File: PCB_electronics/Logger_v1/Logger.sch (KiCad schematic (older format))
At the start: 14 parts, among them P1 GPS_breakout_connector, P2 SD_breakout_connector, U1 MAX232

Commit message: schematic logger seems ok
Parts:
- added C3, C4, C5, C6: 1.0uF, symbol C
- added P10: CONN_01X03, symbol CONN_01X03
- added P11, P12, P13, P? (x2): CONN_01X02, symbol CONN_01X02
- added P8, P9: CONN_01X08, symbol CONN_01X08
- gave numbers to parts that had none: 10
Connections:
- net +5V: now also U1.16 (VCC), P13.1 (P1)
- net GND: now also U1.15 (GND), C5.1, C6.1, P13.2 (P2)
- net MISO: now also P10.3 (P3)
- net MOSI: now also P10.2 (P2)
- net SCK: now also P10.1 (P1)
- net VN_WHITE: now also U1.8 (R2IN)
- net VN_YELLOW: now also U1.7 (T2OUT)
- net ANALOG_8: now reaches XA1.A1
- net ANALOG_8: now also P8.8 (P8)
- net ANALOG_7: now reaches XA1.A2
- net ANALOG_7: now also P8.7 (P7)
- net ANALOG_6: now reaches XA1.A3
- net ANALOG_6: now also P8.6 (P6)
- net ANALOG_5: now reaches XA1.A4
- net ANALOG_5: now also P8.5 (P5)
- net ANALOG_4: now reaches XA1.A5
- net ANALOG_4: now also P8.4 (P4)
- net ANALOG_3: now reaches XA1.A6
- net ANALOG_3: now also P8.3 (P3)
- net ANALOG_2: now reaches XA1.A7
- net ANALOG_2: now also P8.2 (P2)
- net ANALOG_1: now reaches XA1.A8
- net ANALOG_1: now also P8.1 (P1)
- net RX0: now reaches XA1.D0 (D0_RX0)
- net RX0: now also P12.2 (P2)
- net TX0: now reaches XA1.D1 (D1_TX0)
- net TX0: now also P12.1 (P1)
- net TX3: now reaches XA1.D14 (D14_TX3)
- net TX3: now also U1.9 (R2OUT)
- net RX3: now reaches XA1.D15 (D15_RX3)
- net RX3: now also U1.10 (T2IN)
- net DGTL_8: now reaches XA1.D2 (D2_INT0)
- net DGTL_8: now also P9.8 (P8)
- net DGTL_7: now reaches XA1.D3 (D3_INT1)
- net DGTL_7: now also P9.7 (P7)
- net DGTL_6: now reaches XA1.D4
- net DGTL_6: now also P9.6 (P6)
- net DGTL_5: now reaches XA1.D5
- net DGTL_5: now also P9.5 (P5)
- net DGTL_4: now reaches XA1.D6
- net DGTL_4: now also P9.4 (P4)
- net DGTL_3: now reaches XA1.D7
- net DGTL_3: now also P9.3 (P3)
- net DGTL_2: now reaches XA1.D8
- net DGTL_2: now also P9.2 (P2)
- net DGTL_1: now reaches XA1.D9
- net DGTL_1: now also P9.1 (P1)
- net SCL: now reaches XA1.SCL
- net SCL: now also P11.1 (P1)
- net SDA: now reaches XA1.SDA
- net SDA: now also P11.2 (P2)
- net at U1.1 (C1+): now also C3.1
- net at U1.11 (T1IN): now also P?.2 (P2)
- net at U1.12 (R1OUT): now also P?.1 (P1)
- net at U1.13 (R1IN): now also P?.2 (P2)
- net at U1.14 (T1OUT): now also P?.1 (P1)
- net at U1.2 (V+): now also C5.2
- net at U1.3 (C1-): now also C3.2
- net at U1.4 (C2+): now also C4.1
- net at U1.5 (C2-): now also C4.2
- net at U1.6 (V-): now also C6.2
- no-connect marks 17 -> 55
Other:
- note added: "3V_logic_spare"
- note added: "5V_logic_spare"
- note added: "ADC"
- note added: "I2C"
- note added: "SPI"
- note added: "Serial 0\n(for RPi)"
- note added: "TODO: MAX232 and VN100\nTODO: pin headers SPI\nTODO: pin headers I2C\nTODO: a few AnalogPins\nTODO: a few DigitalPins"
- note added: "digital pins"
- note added: "power"
- moved on the sheet: C2, P5, P6, P7, R1, R2, U2

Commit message: schematic logger seems ok
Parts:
- gave numbers to parts that had none: 2
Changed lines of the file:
@@
 NoConn ~ 1300 3600
 $Comp
-L +5V #PWR026
+L +5V #PWR022
 U 1 1 5AF35465
 P 10100 5050
-F 0 "#PWR026" H 10100 4900 50  0001 C CNN
+F 0 "#PWR022" H 10100 4900 50  0001 C CNN
 F 1 "+5V" H 10100 5190 50  0000 C CNN
 F 2 "" H 10100 5050 50  0000 C CNN
@@
 	10100 5050 10250 5050
 $Comp
-L GND #PWR027
+L GND #PWR023
 U 1 1 5AF35551
 P 10100 5150
-F 0 "#PWR027" H 10100 4900 50  0001 C CNN
+F 0 "#PWR023" H 10100 4900 50  0001 C CNN
 F 1 "GND" H 10100 5000 50  0000 C CNN
 F 2 "" H 10100 5150 50  0000 C CNN
@@
 DGTL_8
 $Comp
-L CONN_01X02 P?
+L CONN_01X02 P14
 U 1 1 5AF3A744
 P 4900 6350
-F 0 "P?" H 4900 6500 50  0000 C CNN
+F 0 "P14" H 4900 6500 50  0000 C CNN
 F 1 "CONN_01X02" V 5000 6350 50  0000 C CNN
 F 2 "" H 4900 6350 50  0000 C CNN
@@
 5V_logic_spare
 $Comp
-L CONN_01X02 P?
+L CONN_01X02 P15
 U 1 1 5AF3AA28
 P 8350 6250
-F 0 "P?" H 8350 6400 50  0000 C CNN
+F 0 "P15" H 8350 6400 50  0000 C CNN
 F 1 "CONN_01X02" V 8450 6250 50  0000 C CNN
 F 2 "" H 8350 6250 50  0000 C CNN

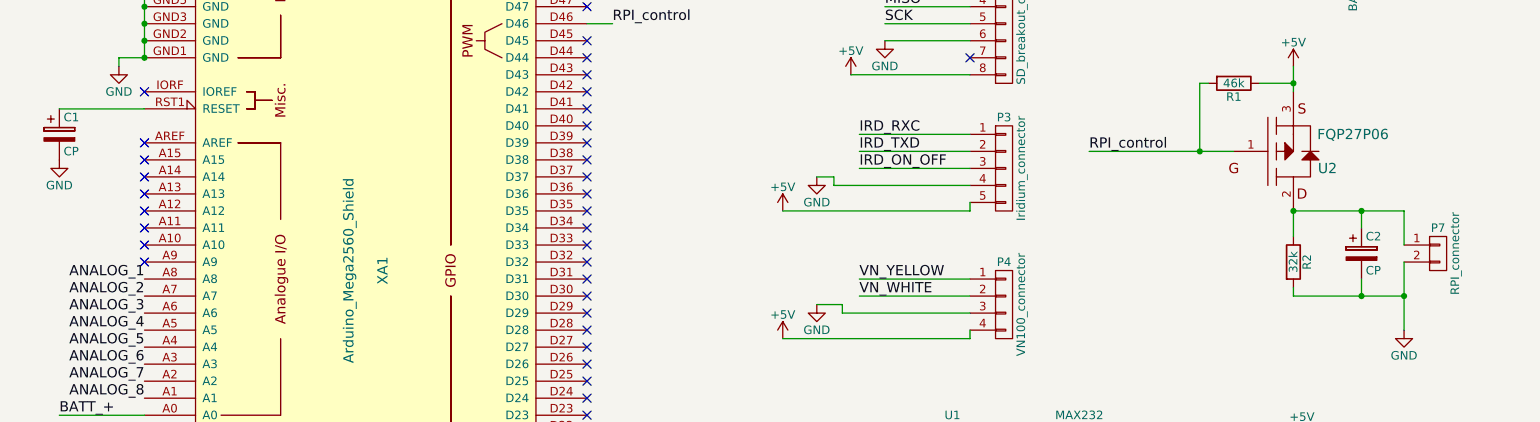
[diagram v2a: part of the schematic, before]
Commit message: placed components 1
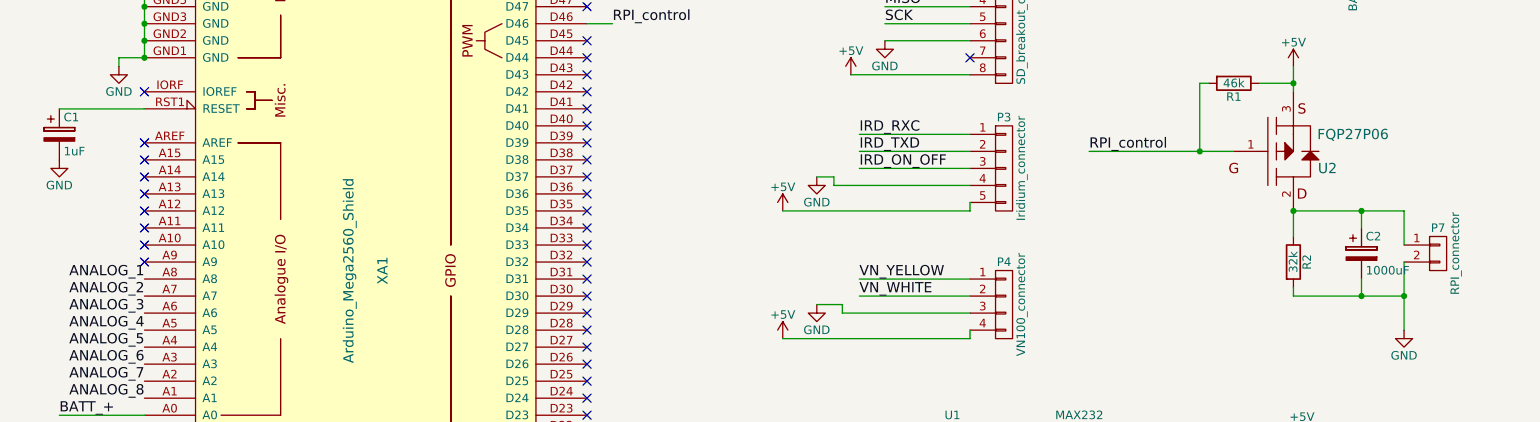
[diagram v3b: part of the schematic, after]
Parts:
- C1: value CP -> 1uF; footprint (none) -> Capacitors_ThroughHole:C_Disc_D3_P2.5
- C2: value CP -> 1000uF; footprint (none) -> Capacitors_ThroughHole:C_Disc_D3_P2.5
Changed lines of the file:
@@
 F 0 "P1" H 6350 1650 50  0000 C CNN
 F 1 "GPS_breakout_connector" V 6450 1150 50  0000 C CNN
-F 2 "" H 6350 1150 50  0000 C CNN
+F 2 "" H 6350 1150 50  0001 C CNN
 F 3 "" H 6350 1150 50  0000 C CNN
 	1    6350 1150
@@
 F 0 "P2" H 6350 2700 50  0000 C CNN
 F 1 "SD_breakout_connector" V 6450 2250 50  0000 C CNN
-F 2 "" H 6350 2250 50  0000 C CNN
+F 2 "" H 6350 2250 50  0001 C CNN
 F 3 "" H 6350 2250 50  0000 C CNN
 	1    6350 2250
@@
 F 0 "U1" H 6000 6300 50  0000 L CNN
 F 1 "MAX232" H 6650 6300 50  0000 L CNN
-F 2 "" H 6450 5450 50  0000 C CNN
+F 2 "" H 6450 5450 50  0001 C CNN
 F 3 "" H 6450 5450 50  0000 C CNN
 	1    6450 5450
@@
 F 0 "U2" H 8250 2950 60  0000 C CNN
 F 1 "FQP27P06" H 8400 3150 60  0000 C CNN
-F 2 "" H 8050 3050 60  0000 C CNN
+F 2 "" H 8050 3050 60  0001 C CNN
 F 3 "" H 8050 3050 60  0000 C CNN
 	1    8050 3050
@@
 P 800 2950
 F 0 "C1" H 825 3050 50  0000 L CNN
-F 1 "CP" H 825 2850 50  0000 L CNN
-F 2 "" H 838 2800 50  0000 C CNN
+F 1 "1uF" H 825 2850 50  0000 L CNN
+F 2 "Capacitors_ThroughHole:C_Disc_D3_P2.5" H 838 2800 50  0001 C CNN
 F 3 "" H 800 2950 50  0000 C CNN
 	1    800  2950
@@
 F 0 "P4" H 6350 4200 50  0000 C CNN
 F 1 "VN100_connector" V 6450 3950 50  0000 C CNN
-F 2 "" H 6350 3950 50  0000 C CNN
+F 2 "" H 6350 3950 50  0001 C CNN
 F 3 "" H 6350 3950 50  0000 C CNN
 	1    6350 3950
@@
 F 0 "P7" H 8900 3800 50  0000 C CNN
 F 1 "RPI_connector" V 9000 3650 50  0000 C CNN
-F 2 "" H 8900 3650 50  0000 C CNN
+F 2 "" H 8900 3650 50  0001 C CNN
 F 3 "" H 8900 3650 50  0000 C CNN
 	1    8900 3650
@@
 F 0 "P5" H 8300 1300 50  0000 C CNN
 F 1 "PowerManager_connector" V 8400 1100 50  0000 C CNN
-F 2 "" H 8300 1100 50  0000 C CNN
+F 2 "" H 8300 1100 50  0001 C CNN
 F 3 "" H 8300 1100 50  0000 C CNN
 	1    8300 1100
@@
 F 0 "P3" H 6350 3450 50  0000 C CNN
 F 1 "Iridium_connector" V 6450 3150 50  0000 C CNN
-F 2 "" H 6350 3150 50  0000 C CNN
+F 2 "" H 6350 3150 50  0001 C CNN
 F 3 "" H 6350 3150 50  0000 C CNN
 	1    6350 3150
@@
 F 0 "P6" H 8300 2050 50  0000 C CNN
 F 1 "BATT_connector" V 8400 1950 50  0000 C CNN
-F 2 "" H 8300 1950 50  0000 C CNN
+F 2 "" H 8300 1950 50  0001 C CNN
 F 3 "" H 8300 1950 50  0000 C CNN
 	1    8300 1950
@@
 P 8450 3650
 F 0 "C2" H 8475 3750 50  0000 L CNN
-F 1 "CP" H 8475 3550 50  0000 L CNN
-F 2 "" H 8488 3500 50  0000 C CNN
+F 1 "1000uF" H 8475 3550 50  0000 L CNN
+F 2 "Capacitors_ThroughHole:C_Disc_D3_P2.5" H 8488 3500 50  0001 C CNN
 F 3 "" H 8450 3650 50  0000 C CNN
 	1    8450 3650
@@
 F 0 "R1" V 7780 2650 50  0000 C CNN
 F 1 "46k" V 7700 2650 50  0000 C CNN
-F 2 "" V 7630 2650 50  0000 C CNN
+F 2 "" V 7630 2650 50  0001 C CNN
 F 3 "" H 7700 2650 50  0000 C CNN
 	1    7700 2650
@@
 F 0 "R2" V 8130 3700 50  0000 C CNN
 F 1 "32k" V 8050 3700 50  0000 C CNN
-F 2 "" V 7980 3700 50  0000 C CNN
+F 2 "" V 7980 3700 50  0001 C CNN
 F 3 "" H 8050 3700 50  0000 C CNN
 	1    8050 3700
@@
 F 0 "P8" H 10450 1700 50  0000 C CNN
 F 1 "CONN_01X08" V 10550 1250 50  0000 C CNN
-F 2 "" H 10450 1250 50  0000 C CNN
+F 2 "" H 10450 1250 50  0001 C CNN
 F 3 "" H 10450 1250 50  0000 C CNN
 	1    10450 1250
@@
 F 0 "P9" H 10450 2800 50  0000 C CNN
 F 1 "CONN_01X08" V 10550 2350 50  0000 C CNN
-F 2 "" H 10450 2350 50  0000 C CNN
+F 2 "" H 10450 2350 50  0001 C CNN
 F 3 "" H 10450 2350 50  0000 C CNN
 	1    10450 2350
@@
 F 0 "P10" H 10450 3400 50  0000 C CNN
 F 1 "CONN_01X03" V 10550 3200 50  0000 C CNN
-F 2 "" H 10450 3200 50  0000 C CNN
+F 2 "" H 10450 3200 50  0001 C CNN
 F 3 "" H 10450 3200 50  0000 C CNN
 	1    10450 3200
@@
 F 0 "P11" H 10450 4000 50  0000 C CNN
 F 1 "CONN_01X02" V 10550 3850 50  0000 C CNN
-F 2 "" H 10450 3850 50  0000 C CNN
+F 2 "" H 10450 3850 50  0001 C CNN
 F 3 "" H 10450 3850 50  0000 C CNN
 	1    10450 3850
@@
 F 0 "P13" H 10450 5250 50  0000 C CNN
 F 1 "CONN_01X02" V 10550 5100 50  0000 C CNN
-F 2 "" H 10450 5100 50  0000 C CNN
+F 2 "" H 10450 5100 50  0001 C CNN
 F 3 "" H 10450 5100 50  0000 C CNN
 	1    10450 5100
@@
 F 0 "C3" H 5475 5050 50  0000 L CNN
 F 1 "1.0uF" H 5475 4850 50  0000 L CNN
-F 2 "" H 5488 4800 50  0000 C CNN
+F 2 "" H 5488 4800 50  0001 C CNN
 F 3 "" H 5450 4950 50  0000 C CNN
 	1    5450 4950
@@
 F 0 "C4" H 5475 5550 50  0000 L CNN
 F 1 "1.0uF" H 5475 5350 50  0000 L CNN
-F 2 "" H 5488 5300 50  0000 C CNN
+F 2 "" H 5488 5300 50  0001 C CNN
 F 3 "" H 5450 5450 50  0000 C CNN
 	1    5450 5450
@@
 F 0 "C5" H 7425 5250 50  0000 L CNN
 F 1 "1.0uF" V 7250 5050 50  0000 L CNN
-F 2 "" H 7438 5000 50  0000 C CNN
+F 2 "" H 7438 5000 50  0001 C CNN
 F 3 "" H 7400 5150 50  0000 C CNN
 	1    7400 5150
@@
 F 0 "C6" H 7425 5750 50  0000 L CNN
 F 1 "1.0uF" V 7250 5550 50  0000 L CNN
-F 2 "" H 7438 5500 50  0000 C CNN
+F 2 "" H 7438 5500 50  0001 C CNN
 F 3 "" H 7400 5650 50  0000 C CNN
 	1    7400 5650
@@
 F 0 "P12" H 10450 4600 50  0000 C CNN
 F 1 "CONN_01X02" V 10550 4450 50  0000 C CNN
-F 2 "" H 10450 4450 50  0000 C CNN
+F 2 "" H 10450 4450 50  0001 C CNN
 F 3 "" H 10450 4450 50  0000 C CNN
 	1    10450 4450
@@
 F 0 "P14" H 4900 6500 50  0000 C CNN
 F 1 "CONN_01X02" V 5000 6350 50  0000 C CNN
-F 2 "" H 4900 6350 50  0000 C CNN
+F 2 "" H 4900 6350 50  0001 C CNN
 F 3 "" H 4900 6350 50  0000 C CNN
 	1    4900 6350
@@
 F 0 "P15" H 8350 6400 50  0000 C CNN
 F 1 "CONN_01X02" V 8450 6250 50  0000 C CNN
-F 2 "" H 8350 6250 50  0000 C CNN
+F 2 "" H 8350 6250 50  0001 C CNN
 F 3 "" H 8350 6250 50  0000 C CNN
 	1    8350 6250

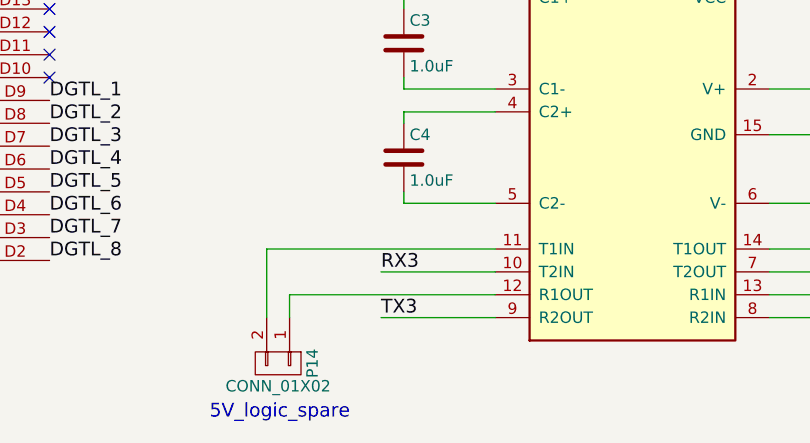
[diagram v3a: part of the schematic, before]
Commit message: corrected error on MAX232
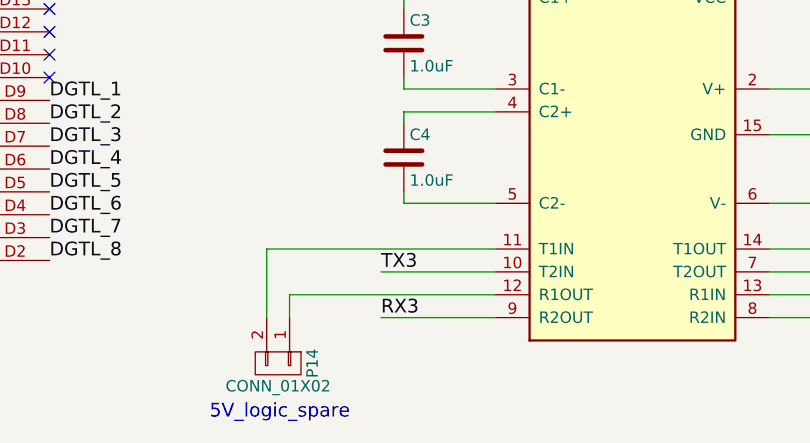
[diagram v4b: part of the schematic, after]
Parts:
- C1: footprint Capacitors_ThroughHole:C_Disc_D3_P2.5 -> Capacitors_ThroughHole:C_Radial_D8_L11.5_P3.5
- C2: footprint Capacitors_ThroughHole:C_Disc_D3_P2.5 -> Capacitors_ThroughHole:C_Radial_D8_L13_P3.8
- C3, C4, C5, C6: footprint (none) -> Capacitors_ThroughHole:C_Disc_D3_P2.5
- P1: footprint (none) -> Pin_Headers:Pin_Header_Straight_1x09
- P10, P5: footprint (none) -> Pin_Headers:Pin_Header_Straight_1x03
- P11, P12, P13, P14, P15, P7: footprint (none) -> Pin_Headers:Pin_Header_Straight_2x01
- P2, P8, P9: footprint (none) -> Pin_Headers:Pin_Header_Straight_1x08
- P3: footprint (none) -> Pin_Headers:Pin_Header_Straight_1x05
- P4: footprint (none) -> Pin_Headers:Pin_Header_Straight_1x04
- P6: footprint (none) -> Pin_Headers:Pin_Header_Straight_1x01
- R1, R2: footprint (none) -> Resistors_ThroughHole:Resistor_Horizontal_RM10mm
- U1: footprint (none) -> Housings_DIP:DIP-16_W7.62mm_LongPads
- U2: footprint (none) -> TO_SOT_Packages_THT:TO-220_Neutral123_Vertical
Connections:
- net RX3: now also U1.9 (R2OUT); no longer U1.10 (T2IN)
- net TX3: now also U1.10 (T2IN); no longer U1.9 (R2OUT)
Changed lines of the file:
@@
 F 0 "P1" H 6350 1650 50  0000 C CNN
 F 1 "GPS_breakout_connector" V 6450 1150 50  0000 C CNN
-F 2 "" H 6350 1150 50  0001 C CNN
+F 2 "Pin_Headers:Pin_Header_Straight_1x09" H 6350 1150 50  0001 C CNN
 F 3 "" H 6350 1150 50  0000 C CNN
 	1    6350 1150
@@
 F 0 "P2" H 6350 2700 50  0000 C CNN
 F 1 "SD_breakout_connector" V 6450 2250 50  0000 C CNN
-F 2 "" H 6350 2250 50  0001 C CNN
+F 2 "Pin_Headers:Pin_Header_Straight_1x08" H 6350 2250 50  0001 C CNN
 F 3 "" H 6350 2250 50  0000 C CNN
 	1    6350 2250
@@
 F 0 "U1" H 6000 6300 50  0000 L CNN
 F 1 "MAX232" H 6650 6300 50  0000 L CNN
-F 2 "" H 6450 5450 50  0001 C CNN
+F 2 "Housings_DIP:DIP-16_W7.62mm_LongPads" H 6450 5450 50  0001 C CNN
 F 3 "" H 6450 5450 50  0000 C CNN
 	1    6450 5450
@@
 F 0 "U2" H 8250 2950 60  0000 C CNN
 F 1 "FQP27P06" H 8400 3150 60  0000 C CNN
-F 2 "" H 8050 3050 60  0001 C CNN
+F 2 "TO_SOT_Packages_THT:TO-220_Neutral123_Vertical" H 8050 3050 60  0001 C CNN
 F 3 "" H 8050 3050 60  0000 C CNN
 	1    8050 3050
@@
 F 0 "C1" H 825 3050 50  0000 L CNN
 F 1 "1uF" H 825 2850 50  0000 L CNN
-F 2 "Capacitors_ThroughHole:C_Disc_D3_P2.5" H 838 2800 50  0001 C CNN
+F 2 "Capacitors_ThroughHole:C_Radial_D8_L11.5_P3.5" H 838 2800 50  0001 C CNN
 F 3 "" H 800 2950 50  0000 C CNN
 	1    800  2950
@@
 F 0 "P4" H 6350 4200 50  0000 C CNN
 F 1 "VN100_connector" V 6450 3950 50  0000 C CNN
-F 2 "" H 6350 3950 50  0001 C CNN
+F 2 "Pin_Headers:Pin_Header_Straight_1x04" H 6350 3950 50  0001 C CNN
 F 3 "" H 6350 3950 50  0000 C CNN
 	1    6350 3950
@@
 F 0 "P7" H 8900 3800 50  0000 C CNN
 F 1 "RPI_connector" V 9000 3650 50  0000 C CNN
-F 2 "" H 8900 3650 50  0001 C CNN
+F 2 "Pin_Headers:Pin_Header_Straight_2x01" H 8900 3650 50  0001 C CNN
 F 3 "" H 8900 3650 50  0000 C CNN
 	1    8900 3650
@@
 F 0 "P5" H 8300 1300 50  0000 C CNN
 F 1 "PowerManager_connector" V 8400 1100 50  0000 C CNN
-F 2 "" H 8300 1100 50  0001 C CNN
+F 2 "Pin_Headers:Pin_Header_Straight_1x03" H 8300 1100 50  0001 C CNN
 F 3 "" H 8300 1100 50  0000 C CNN
 	1    8300 1100
@@
 F 0 "P3" H 6350 3450 50  0000 C CNN
 F 1 "Iridium_connector" V 6450 3150 50  0000 C CNN
-F 2 "" H 6350 3150 50  0001 C CNN
+F 2 "Pin_Headers:Pin_Header_Straight_1x05" H 6350 3150 50  0001 C CNN
 F 3 "" H 6350 3150 50  0000 C CNN
 	1    6350 3150
@@
 F 0 "P6" H 8300 2050 50  0000 C CNN
 F 1 "BATT_connector" V 8400 1950 50  0000 C CNN
-F 2 "" H 8300 1950 50  0001 C CNN
+F 2 "Pin_Headers:Pin_Header_Straight_1x01" H 8300 1950 50  0001 C CNN
 F 3 "" H 8300 1950 50  0000 C CNN
 	1    8300 1950
@@
 F 0 "C2" H 8475 3750 50  0000 L CNN
 F 1 "1000uF" H 8475 3550 50  0000 L CNN
-F 2 "Capacitors_ThroughHole:C_Disc_D3_P2.5" H 8488 3500 50  0001 C CNN
+F 2 "Capacitors_ThroughHole:C_Radial_D8_L13_P3.8" H 8488 3500 50  0001 C CNN
 F 3 "" H 8450 3650 50  0000 C CNN
 	1    8450 3650
@@
 F 0 "R1" V 7780 2650 50  0000 C CNN
 F 1 "46k" V 7700 2650 50  0000 C CNN
-F 2 "" V 7630 2650 50  0001 C CNN
+F 2 "Resistors_ThroughHole:Resistor_Horizontal_RM10mm" V 7630 2650 50  0001 C CNN
 F 3 "" H 7700 2650 50  0000 C CNN
 	1    7700 2650
@@
 F 0 "R2" V 8130 3700 50  0000 C CNN
 F 1 "32k" V 8050 3700 50  0000 C CNN
-F 2 "" V 7980 3700 50  0001 C CNN
+F 2 "Resistors_ThroughHole:Resistor_Horizontal_RM10mm" V 7980 3700 50  0001 C CNN
 F 3 "" H 8050 3700 50  0000 C CNN
 	1    8050 3700
@@
 F 0 "P8" H 10450 1700 50  0000 C CNN
 F 1 "CONN_01X08" V 10550 1250 50  0000 C CNN
-F 2 "" H 10450 1250 50  0001 C CNN
+F 2 "Pin_Headers:Pin_Header_Straight_1x08" H 10450 1250 50  0001 C CNN
 F 3 "" H 10450 1250 50  0000 C CNN
 	1    10450 1250
@@
 F 0 "P9" H 10450 2800 50  0000 C CNN
 F 1 "CONN_01X08" V 10550 2350 50  0000 C CNN
-F 2 "" H 10450 2350 50  0001 C CNN
+F 2 "Pin_Headers:Pin_Header_Straight_1x08" H 10450 2350 50  0001 C CNN
 F 3 "" H 10450 2350 50  0000 C CNN
 	1    10450 2350
@@
 F 0 "P10" H 10450 3400 50  0000 C CNN
 F 1 "CONN_01X03" V 10550 3200 50  0000 C CNN
-F 2 "" H 10450 3200 50  0001 C CNN
+F 2 "Pin_Headers:Pin_Header_Straight_1x03" H 10450 3200 50  0001 C CNN
 F 3 "" H 10450 3200 50  0000 C CNN
 	1    10450 3200
@@
 F 0 "P11" H 10450 4000 50  0000 C CNN
 F 1 "CONN_01X02" V 10550 3850 50  0000 C CNN
-F 2 "" H 10450 3850 50  0001 C CNN
+F 2 "Pin_Headers:Pin_Header_Straight_2x01" H 10450 3850 50  0001 C CNN
 F 3 "" H 10450 3850 50  0000 C CNN
 	1    10450 3850
@@
 F 0 "P13" H 10450 5250 50  0000 C CNN
 F 1 "CONN_01X02" V 10550 5100 50  0000 C CNN
-F 2 "" H 10450 5100 50  0001 C CNN
+F 2 "Pin_Headers:Pin_Header_Straight_2x01" H 10450 5100 50  0001 C CNN
 F 3 "" H 10450 5100 50  0000 C CNN
 	1    10450 5100
@@
 	700  5200 1300 5200
 Text Label 5350 5950 0    60   ~ 0
-RX3
+TX3
 Wire Wire Line
 	5350 5950 5850 5950
 Text Label 5350 6150 0    60   ~ 0
-TX3
+RX3
 Wire Wire Line
 	5350 6150 5850 6150
@@
 F 0 "C3" H 5475 5050 50  0000 L CNN
 F 1 "1.0uF" H 5475 4850 50  0000 L CNN
-F 2 "" H 5488 4800 50  0001 C CNN
+F 2 "Capacitors_ThroughHole:C_Disc_D3_P2.5" H 5488 4800 50  0001 C CNN
 F 3 "" H 5450 4950 50  0000 C CNN
 	1    5450 4950
@@
 F 0 "C4" H 5475 5550 50  0000 L CNN
 F 1 "1.0uF" H 5475 5350 50  0000 L CNN
-F 2 "" H 5488 5300 50  0001 C CNN
+F 2 "Capacitors_ThroughHole:C_Disc_D3_P2.5" H 5488 5300 50  0001 C CNN
 F 3 "" H 5450 5450 50  0000 C CNN
 	1    5450 5450
@@
 F 0 "C5" H 7425 5250 50  0000 L CNN
 F 1 "1.0uF" V 7250 5050 50  0000 L CNN
-F 2 "" H 7438 5000 50  0001 C CNN
+F 2 "Capacitors_ThroughHole:C_Disc_D3_P2.5" H 7438 5000 50  0001 C CNN
 F 3 "" H 7400 5150 50  0000 C CNN
 	1    7400 5150
@@
 F 0 "C6" H 7425 5750 50  0000 L CNN
 F 1 "1.0uF" V 7250 5550 50  0000 L CNN
-F 2 "" H 7438 5500 50  0001 C CNN
+F 2 "Capacitors_ThroughHole:C_Disc_D3_P2.5" H 7438 5500 50  0001 C CNN
 F 3 "" H 7400 5650 50  0000 C CNN
 	1    7400 5650
@@
 F 0 "P12" H 10450 4600 50  0000 C CNN
 F 1 "CONN_01X02" V 10550 4450 50  0000 C CNN
-F 2 "" H 10450 4450 50  0001 C CNN
+F 2 "Pin_Headers:Pin_Header_Straight_2x01" H 10450 4450 50  0001 C CNN
 F 3 "" H 10450 4450 50  0000 C CNN
 	1    10450 4450
@@
 F 0 "P14" H 4900 6500 50  0000 C CNN
 F 1 "CONN_01X02" V 5000 6350 50  0000 C CNN
-F 2 "" H 4900 6350 50  0001 C CNN
+F 2 "Pin_Headers:Pin_Header_Straight_2x01" H 4900 6350 50  0001 C CNN
 F 3 "" H 4900 6350 50  0000 C CNN
 	1    4900 6350
@@
 F 0 "P15" H 8350 6400 50  0000 C CNN
 F 1 "CONN_01X02" V 8450 6250 50  0000 C CNN
-F 2 "" H 8350 6250 50  0001 C CNN
+F 2 "Pin_Headers:Pin_Header_Straight_2x01" H 8350 6250 50  0001 C CNN
 F 3 "" H 8350 6250 50  0000 C CNN
 	1    8350 6250
